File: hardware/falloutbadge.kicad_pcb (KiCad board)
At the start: 2 copper layers, 86 x 98 mm, 106 parts, among them J1 LiPo, J3 USB_C_Receptacle_USB2.0_16P, J4 E-INK, J5 Conn_01x03, Q2 Si1308EDL, Q3 AO3400A, SW1 SW_Push, SW2 SW_Push, SW3 SW_Push, SW4 SW_Push, SW5 SW_Push, T1 BALFLB-WL-09D3, U1 CH592F, U2 STM32WLE5CCUx, U3 CH9102F, U4 USBLC6-2SC6, U6 BGS12SN6, U7 AP2112K-3.3, U8 TP4056-42-ESOP8, Y1 32MHz, Y2 32MHz

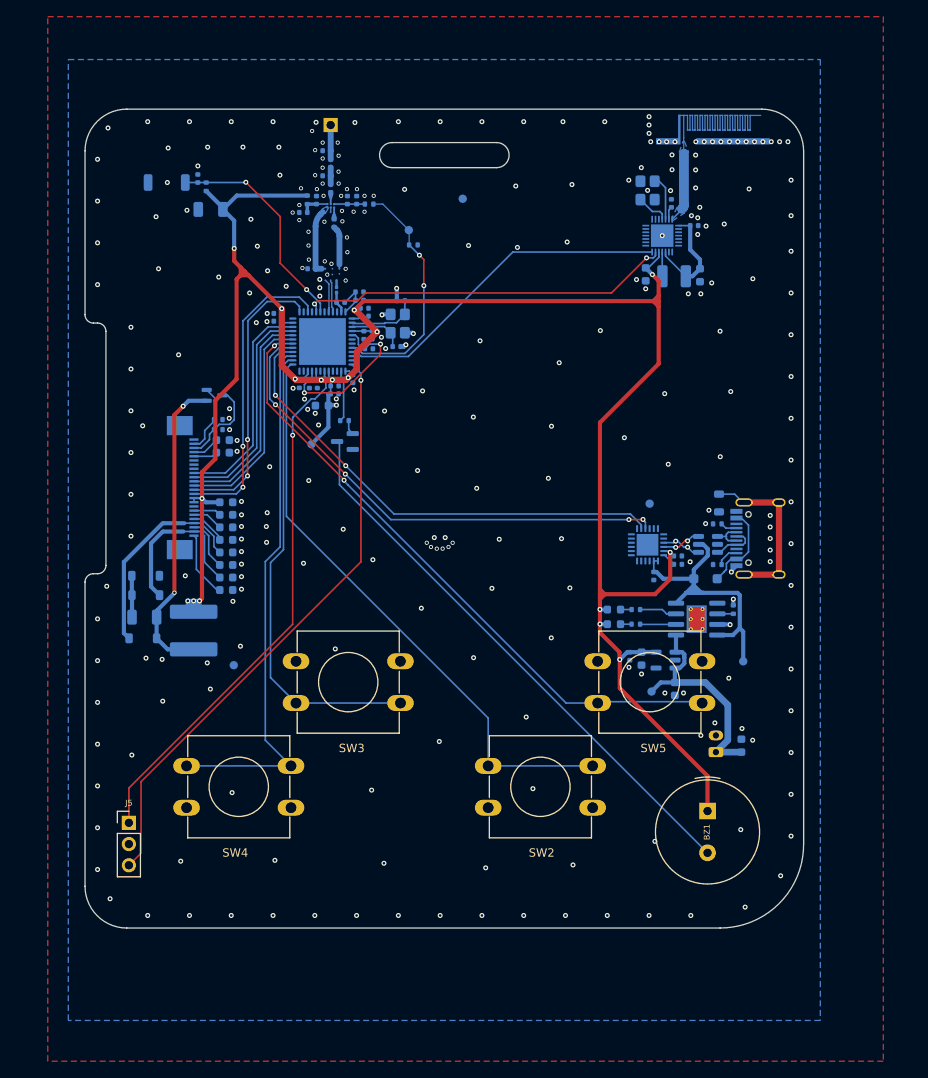
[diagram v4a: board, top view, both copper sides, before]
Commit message: add v2 w/o lora
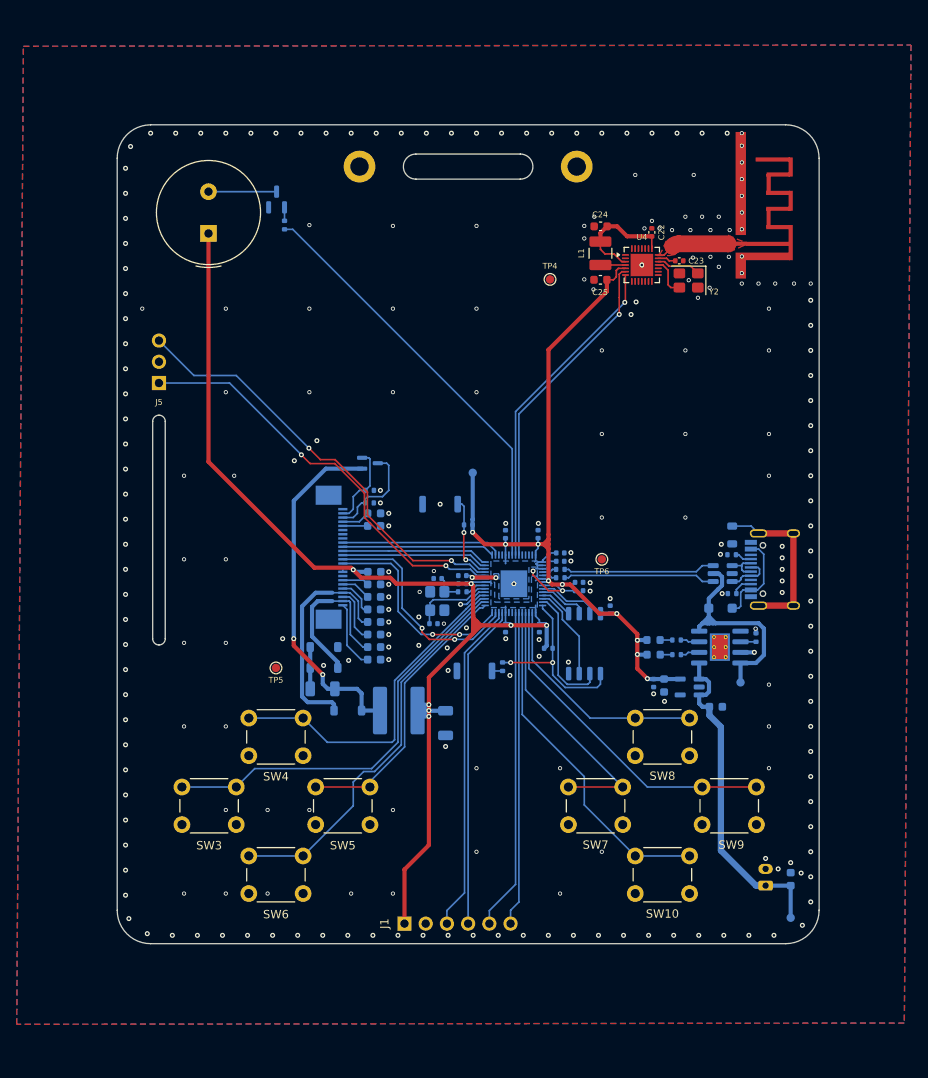
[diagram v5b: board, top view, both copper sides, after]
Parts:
- removed AE3: Antenna_Shield, antenna:ANT-F-1-2.4G-0.8mmFR4-WCH
- removed C14, C17, C18, C47, C49, C53, C54: 100nF, Capacitor_SMD:C_0402_1005Metric
- removed C19: 10uF, Capacitor_SMD:C_0603_1608Metric
- removed C20: 4.7uF, Capacitor_SMD:C_1206_3216Metric
- removed C21, C50, C52: 1uF, Capacitor_SMD:C_0402_1005Metric
- removed C42, C46, C48: 4.7uF, Capacitor_SMD:C_0603_1608Metric
- removed C43, C45: 2.2pF, Capacitor_SMD:C_0402_1005Metric
- removed C44: 1nF, Capacitor_SMD:C_0402_1005Metric
- removed C51: NC, Capacitor_SMD:C_0402_1005Metric
- removed C7: 47nF, Capacitor_SMD:C_0402_1005Metric
- removed C9: 2.2uF, Capacitor_SMD:C_0603_1608Metric
- removed D1, D2: MBR0530, Diode_SMD:D_SOD-123
- removed D4: D, Diode_SMD:D_SOD-123F
- removed D7: RED, LED_SMD:LED_0603_1608Metric
- removed L3: 68uH, Inductor_SMD:L_Changjiang_FNR6028S
- removed L4: 6.8uH, Inductor_SMD:L_0402_1005Metric
- removed L6: 10uH, Inductor_SMD:L_1210_3225Metric
- removed Q3: AO3400A, Package_TO_SOT_SMD:SOT-23
- removed R16, R17: 100R, Resistor_SMD:R_0402_1005Metric
- removed R8: 5.1k, Resistor_SMD:R_0402_1005Metric
- removed T1: BALFLB-WL-09D3, falloutbadge:CSPG-8_L2.1-W1.8_BALFHB-WL-03D3
- removed TP7: CTRL, TestPoint:TestPoint_Pad_D1.0mm
- removed U3: CH9102F, Package_DFN_QFN:QFN-24-1EP_4x4mm_P0.5mm_EP2.6x2.6mm
- removed U8: TP4056-42-ESOP8, Package_SO:SOIC-8-1EP_3.9x4.9mm_P1.27mm_EP2.41x3.3mm_ThermalVias
- added C13: 100nF, Capacitor_SMD:C_0402_1005Metric, B.Cu at (153.5, 102.0)
- added C35: 1uF, Capacitor_SMD:C_0603_1608Metric, B.Cu at (137.8, 114.0)
- added D10: MBR0530, Diode_SMD:D_SOD-123, B.Cu at (131.8, 118.0)
- added D11: MBR0530, Diode_SMD:D_SOD-123, B.Cu at (134.6, 123.1)
- added D6: RED, LED_SMD:LED_0603_1608Metric, B.Cu at (171.2, 114.7)
- added D9: MBR0530, Diode_SMD:D_SOD-123, B.Cu at (131.8, 115.5)
- added H1: MountingHole, MountingHole:MountingHole_2.2mm_M2_DIN965_Pad, F.Cu at (136.0, 58.0)
- added H2: MountingHole, MountingHole:MountingHole_2.2mm_M2_DIN965_Pad, F.Cu at (162.0, 58.0)
- added J2: USB_C_Receptacle_USB2.0_16P, Connector_USB:USB_C_Receptacle_HRO_TYPE-C-31-M-12, B.Cu at (186.9, 106.2)
- added L2: 68uH, Inductor_SMD:L_Changjiang_FNR6028S, B.Cu at (140.7, 123.1)
- added Q1: AO3400A, Package_TO_SOT_SMD:SOT-23, B.Cu at (126.1, 61.9)
- added R10: 5.1k, Resistor_SMD:R_0402_1005Metric, B.Cu at (180.6, 109.1)
- added R11: 10k, Resistor_SMD:R_0402_1005Metric, B.Cu at (137.2, 96.8)
- added R14: 330R, Resistor_SMD:R_0402_1005Metric, B.Cu at (173.9, 116.4)
- added R3: 1k, Resistor_SMD:R_0402_1005Metric, B.Cu at (148.3, 108.9)
- added R5: 27.4R, Resistor_SMD:R_0402_1005Metric, B.Cu at (160.0, 107.2)
- added SW10: SW_Push, Button_Switch_THT:SW_PUSH_6mm, F.Cu at (169.0, 140.5)
- added SW6: SW_Push, Button_Switch_THT:SW_PUSH_6mm, F.Cu at (122.8, 140.5)
- added SW7: SW_Push, Button_Switch_THT:SW_PUSH_6mm, F.Cu at (161.0, 132.2)
- added SW8: SW_Push, Button_Switch_THT:SW_PUSH_6mm, F.Cu at (169.0, 124.0)
- added SW9: SW_Push, Button_Switch_THT:SW_PUSH_6mm, F.Cu at (177.0, 132.2)
- added U5: USBLC6-2SC6, Package_TO_SOT_SMD:SOT-23-6, B.Cu at (179.5, 106.7)
- AE2: value Antenna -> Antenna_Shield; footprint Connector_PinHeader_2.54mm:PinHeader_1x01_P2.54mm_Vertical -> antenna:ANT-F-1-2.4G-1.6mmFR4-WCH; moved to F.Cu
- C1, C2: value 100nF -> 33pF
- C10: value 4.7uF -> 100nF; footprint Capacitor_SMD:C_0603_1608Metric -> Capacitor_SMD:C_0402_1005Metric
- C11: value 1uF -> 100nF
- C22: value 4.7uF -> 100nF; footprint Capacitor_SMD:C_1206_3216Metric -> Capacitor_SMD:C_0402_1005Metric; moved to F.Cu
- C23: value 100nF -> 0.47uF; moved to F.Cu
- C24: value 1uF -> 4.7uF; moved to F.Cu
- C25: value 1uF -> 2.2uF; moved to F.Cu
- C26, C27: value 1uF -> 4.7uF; footprint Capacitor_SMD:C_0603_1608Metric -> Capacitor_SMD:C_1206_3216Metric
- C3: value 0.47uF -> 100nF
- C34: value 100nF -> 1uF; footprint Capacitor_SMD:C_0402_1005Metric -> Capacitor_SMD:C_0603_1608Metric
- C36: value 100pF -> 1uF; footprint Capacitor_SMD:C_0201_0603Metric -> Capacitor_SMD:C_0603_1608Metric
- C37: value 68pF -> 1uF; footprint Capacitor_SMD:C_0402_1005Metric -> Capacitor_SMD:C_0603_1608Metric
- C38: value 10pF -> 4.7uF; footprint Capacitor_SMD:C_0402_1005Metric -> Capacitor_SMD:C_0603_1608Metric
- C39: value 10pF -> 10uF; footprint Capacitor_SMD:C_0402_1005Metric -> Capacitor_SMD:C_0603_1608Metric
- C40: value 1nF -> 4.7uF; footprint Capacitor_SMD:C_0402_1005Metric -> Capacitor_SMD:C_0603_1608Metric
- C41: value 68pF -> 100nF
- C5: value 6.8pF -> 100nF
- C6: value 6.8pF -> 1uF
- C8: value 68pF -> 1uF
- D3: value MBR0530 -> D; footprint Diode_SMD:D_SOD-123 -> Diode_SMD:D_SOD-123F
- J1: value LiPo -> Conn_02x03; footprint Connector_JST:JST_PH_S2B-PH-K_1x02_P2.00mm_Horizontal -> Connector_PinHeader_2.54mm:PinHeader_1x06_P2.54mm_Vertical; moved to F.Cu
- J3: value USB_C_Receptacle_USB2.0_16P -> E-INK; footprint Connector_USB:USB_C_Receptacle_HRO_TYPE-C-31-M-12 -> Connector_FFC-FPC:TE_2-1734839-4_1x24-1MP_P0.5mm_Horizontal
- J4: value E-INK -> LiPo; footprint Connector_FFC-FPC:TE_2-1734839-4_1x24-1MP_P0.5mm_Horizontal -> Connector_JST:JST_PH_S2B-PH-K_1x02_P2.00mm_Horizontal
- L1: value 68nH -> 10uH; footprint Inductor_SMD:L_0402_1005Metric -> Inductor_SMD:L_1210_3225Metric; moved to F.Cu
- R1: value 10k -> 330R
- R12: value 330R -> 0.47R
- R2: value 330R -> 10k
- R4: value 10k -> 27.4R
- R7: value 0.47R -> 1k
- SW1: value SW_Push -> RESET; footprint Button_Switch_SMD:SW_SPST_TS-1088-xR025 -> Button_Switch_SMD:SW_Push_SPST_NO_Alps_SKRK
- SW2: value SW_Push -> BOOTSEL; footprint Button_Switch_THT:SW_PUSH-12mm -> Button_Switch_SMD:SW_Push_SPST_NO_Alps_SKRK; moved to B.Cu
- SW3, SW4, SW5: footprint Button_Switch_THT:SW_PUSH-12mm -> Button_Switch_THT:SW_PUSH_6mm
- TP2: value GND -> VBUS
- TP3: value VBUS -> +BATT
- TP4, TP6, Y2: moved to F.Cu
- TP5: value +BATT -> GND; moved to F.Cu
- U1: value CH592F -> W25Q32JVSS; footprint Package_DFN_QFN:WQFN-28-1EP_4x4mm_P0.4mm_EP2.7x2.7mm -> Package_SO:SOIC-8_5.3x5.3mm_P1.27mm
- U2: value STM32WLE5CCUx -> RP2040; footprint footprints:UFQFPN-48_L7.0-W7.0-P0.50-BL-EP5.6 -> Package_DFN_QFN:QFN-56-1EP_7x7mm_P0.4mm_EP3.2x3.2mm
- U4: value USBLC6-2SC6 -> CH592F; footprint Package_TO_SOT_SMD:SOT-23-6 -> Package_DFN_QFN:WQFN-28-1EP_4x4mm_P0.4mm_EP2.7x2.7mm; moved to F.Cu
- U6: value BGS12SN6 -> TP4056-42-ESOP8; footprint Package_LGA:Infineon_PG-TSNP-6-10_0.7x1.1mm_0.7x1.1mm_P0.4mm -> Package_SO:SOIC-8-1EP_3.9x4.9mm_P1.27mm_EP2.41x3.3mm_ThermalVias
- Y1: value 32MHz -> 12MHz
- moved C39 97.0 mm to (187.6, 143.3)
- moved BZ1 91.4 mm to (117.9, 66.0), turned to 90 degrees
- moved J4 84.5 mm to (184.6, 144.1)
- moved C38 77.2 mm to (178.7, 122.7), turned to 180 degrees
- moved C22 76.2 mm to (171.0, 65.9), turned to -90 degrees
- moved C4 71.4 mm to (166.0, 111.0), turned to 90 degrees
- moved C40 71.2 mm to (172.4, 120.1), turned to 90 degrees
- moved C41 70.7 mm to (171.2, 119.8)
- moved U6 70.4 mm to (179.1, 115.5), turned to 180 degrees
- moved D3 69.2 mm to (179.2, 110.8)
- moved C24 55.7 mm to (164.9, 65.2)
- moved J5 52.8 mm to (112.0, 83.9), turned to 180 degrees
- moved J3 52.5 mm to (132.7, 104.8), turned to 90 degrees
- moved C37 52.4 mm to (137.8, 117.0), turned to 180 degrees
- moved C2 52.2 mm to (145.4, 107.3), turned to 0 degrees
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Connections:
- C1 pad 1: +3V3 -> GND
- C1 pad 2: GND -> Net-(U2-XIN)
- C10 pad 1: /VDCIA -> +3V3
- C12 pad 1: GND -> +3V3
- C12 pad 2: /VFBSMPS -> GND
- C16 pad 1: /VFBSMPS -> +3V3
- C2 pad 2: /VDCIA -> Net-(C2-Pad2)
- C22 pad 1: Net-(D1-A) -> GND
- C22 pad 2: Net-(D3-A) -> /VDCIA
- C23 pad 1: Net-(U3-V3) -> GND
- C23 pad 2: GND -> Net-(U4-VINTA)
- C24 pad 1: GND -> /VDCIA
- C24 pad 2: +3V3 -> GND
- C25 pad 2: Net-(J4-Pin_21) -> +3V3
- C26 pad 1: GND -> +3V3
- C26 pad 2: Net-(J4-Pin_20) -> GND
- C27 pad 1: GND -> Net-(D10-K)
- C27 pad 2: Net-(J4-Pin_7) -> Net-(D11-A)
- C28 pad 2: Net-(J4-Pin_6) -> +3V3
- C29 pad 2: Net-(J4-Pin_5) -> Net-(J3-Pin_21)
- C3 pad 1: GND -> +1V1
- C3 pad 2: Net-(U1-VINTA) -> GND
- C30 pad 2: /PREVGH -> Net-(J3-Pin_20)
- C31 pad 2: Net-(J4-Pin_3) -> Net-(J3-Pin_7)
- C32 pad 2: /PREVGL -> Net-(J3-Pin_6)
- C33 pad 2: Net-(J4-Pin_1) -> Net-(J3-Pin_5)
- C34 pad 1: +3V3 -> GND
- C34 pad 2: GND -> /PREVGH
- C36 pad 1: /RFO_HP -> GND
- C36 pad 2: Net-(T1-RFO_in) -> /PREVGL
- C37 pad 1: Net-(U6-RF2) -> GND
- C37 pad 2: /C1 -> Net-(J3-Pin_1)
- C38 pad 1: Net-(U6-VDD) -> GND
- C38 pad 2: GND -> +BATT
- C39 pad 1: Net-(U6-CTRL) -> +BATT
- C4 pad 1: GND -> +3V3
- C4 pad 2: Net-(U2-NRST) -> GND
- C40 pad 1: Net-(U6-VDD) -> GND
- C40 pad 2: GND -> +3V3
- C41 pad 1: Net-(C41-Pad1) -> +3V3
- C41 pad 2: Net-(U6-RFIN) -> GND
- C5 pad 1: GND -> +1V1
- C5 pad 2: Net-(U2-OSC_IN) -> GND
- C6 pad 1: GND -> +1V1
- C6 pad 2: Net-(U2-OSC_OUT) -> GND
- C8 pad 1: GND -> +3V3
- C8 pad 2: /VR_PA -> GND
- D3 pad 1: /PREVGH -> VBUS
- FB1 pad 1: Net-(J3-SHIELD) -> Net-(J2-SHIELD)
- J1 pad 1: +BATT -> +3V3
- J4 pad 1: Net-(J4-Pin_1) -> +BATT
- J4 pad 2: /PREVGL -> GND
- L1 pad 1: /VR_PA -> /VSW
- L1 pad 2: /RFO_HP -> /VDCIA
- Q2 pad 1: Net-(D3-A) -> Net-(D11-A)
- R1 pad 1: +3V3 -> /BUZ
- R1 pad 2: Net-(U2-NRST) -> Net-(Q1-G)
- R12 pad 1: Net-(D7-K) -> /RESE
- R12 pad 2: Net-(U8-~{CHRG}) -> GND
- R13 pad 1: Net-(D8-K) -> Net-(D6-K)
- R13 pad 2: Net-(U8-~{STDBY}) -> Net-(U6-~{CHRG})
- R15 pad 1: Net-(U8-PROG) -> Net-(U6-PROG)
- R2 pad 1: /PC13 -> +3V3
- R2 pad 2: Net-(Q3-G) -> Net-(U2-RUN)
- R4 pad 1: /CTRL -> /D-
- R4 pad 2: GND -> Net-(U2-USB_DM)
- R6 pad 1: /GDR -> +3V3
- R6 pad 2: GND -> /QSPI_SS
- R7 pad 1: /RESE -> Net-(R7-Pad1)
- R7 pad 2: GND -> /QSPI_SS
- R9 pad 1: Net-(J3-CC2) -> Net-(J2-CC1)
- SW1 pad 2: Net-(U2-NRST) -> Net-(U2-RUN)
- SW2 pad 1: /PB3 -> GND
- SW2 pad 2: GND -> Net-(R7-Pad1)
- SW3 pad 1: /PB4 -> /BTN1
- SW4 pad 1: /PB5 -> /BTN2
- SW5 pad 1: /PB8 -> /BTN3
- TP2 pad 1: GND -> VBUS
- TP3 pad 1: VBUS -> +BATT
- TP5 pad 1: +BATT -> GND
- U1 pad 1: unconnected-(U1-PA11-Pad1) -> /QSPI_SS
- U1 pad 2: unconnected-(U1-PA10-Pad2) -> /QSPI_SD1
- U1 pad 3: /VDCIA -> /QSPI_SD2
- U1 pad 4: /VSW -> GND
- U1 pad 5: +3V3 -> /QSPI_SD0
- U1 pad 6: /UART1_RX -> /QSPI_SCK
- U1 pad 7: /UART1_TX -> /QSPI_SD3
- U1 pad 8: unconnected-(U1-PB15-Pad8) -> +3V3
- U2 pad 1: /PB3 -> +3V3
- U2 pad 10: /BUSY -> +3V3
- U2 pad 11: +3V3 -> /SDA
- U2 pad 12: unconnected-(U2-PA4-Pad12) -> /SCL
- U2 pad 14: unconnected-(U2-PA6-Pad14) -> /SPI_MOSI
- U2 pad 15: /SPI_MOSI -> /BTN3
- U2 pad 16: unconnected-(U2-PA8-Pad16) -> /BTN4
- U2 pad 17: /UART1_RX -> /BTN1
- U2 pad 18: Net-(U2-NRST) -> /BTN2
- U2 pad 19: unconnected-(U2-PH3-Pad19) -> GND
- U2 pad 2: /PB4 -> /BTN6
- U2 pad 20: /RFI_P -> Net-(U2-XIN)
- U2 pad 21: /RFI_N -> Net-(U2-XOUT)
- U2 pad 22: unconnected-(U2-RFO_LP-Pad22) -> +3V3
- U2 pad 23: /RFO_HP -> +1V1
- U2 pad 24: /VR_PA -> /SWCLK
- U2 pad 25: +3V3 -> /SWDIO
- U2 pad 26: Net-(U2-OSC_IN) -> Net-(U2-RUN)
- U2 pad 27: Net-(U2-OSC_OUT) -> /CS
- U2 pad 28: +3V3 -> /DC
- U2 pad 29: /VFBSMPS -> /RST
- U2 pad 3: /PB5 -> /BTN7
- U2 pad 30: unconnected-(U2-PB0-Pad30) -> /BUSY
- U2 pad 31: unconnected-(U2-PB2-Pad31) -> GND
- U2 pad 32: /CTRL -> unconnected-(U2-GPIO21-Pad32)
- U2 pad 33: /UART1_TX -> +3V3
- U2 pad 35: unconnected-(U2-PA12-Pad35) -> /BUZ
- U2 pad 36: /SWDIO -> /UART1_TX
- U2 pad 37: +3V3 -> /UART1_RX
- U2 pad 38: /PC13 -> unconnected-(U2-GPIO26/ADC0-Pad38)
- U2 pad 4: /RXD -> /BTN5
- U2 pad 41: +3V3 -> unconnected-(U2-GPIO29/ADC3-Pad41)
- U2 pad 42: /SWCLK -> +3V3
- U2 pad 43: unconnected-(U2-PA15-Pad43) -> +3V3
- U2 pad 45: /VFBSMPS -> +1V1
- U2 pad 46: +3V3 -> Net-(U2-USB_DM)
- U2 pad 47: unconnected-(U2-VLXSMPS-Pad47) -> Net-(U2-USB_DP)
- U2 pad 48: GND -> +3V3
- U2 pad 49: GND -> +3V3
- U2 pad 5: /TXD -> /BTN8
- U2 pad 6: /PB8 -> /GPIO4
- U2 pad 7: /CS -> /GPIO5
- U2 pad 8: /DC -> unconnected-(U2-GPIO6-Pad8)
- U2 pad 9: /RST -> unconnected-(U2-GPIO7-Pad9)
- U4 pad 1: Net-(J3-D--PadA7) -> unconnected-(U4-PA11-Pad1)
- U4 pad 2: GND -> unconnected-(U4-PA10-Pad2)
- U4 pad 3: Net-(J3-D+-PadA6) -> /VDCIA
- U4 pad 4: /D+ -> /VSW
- U4 pad 5: VBUS -> +3V3
- U4 pad 6: /D- -> /UART1_RX
- U6 pad 1: Net-(U6-RF2) -> GND
- U6 pad 2: GND -> Net-(U6-PROG)
- U6 pad 3: Net-(T1-RFI_in) -> GND
- U6 pad 4: Net-(U6-VDD) -> VBUS
- U6 pad 5: Net-(U6-RFIN) -> +BATT
- U6 pad 6: Net-(U6-CTRL) -> Net-(U6-~{STDBY})
- Y1 pad 1: Net-(U2-OSC_IN) -> Net-(U2-XIN)
- Y1 pad 3: Net-(U2-OSC_OUT) -> Net-(C2-Pad2)
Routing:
- net /PB8: track 76.6 -> 0.00 mm, vias 2 -> 0
- net /PB3: track 71.0 -> 0.00 mm
- net /PB5: track 64.6 -> 0.00 mm
- net /TXD: track 60.1 -> 0.00 mm, vias 4 -> 0
- net Net-(BZ1--): track 67.6 -> 8.15 mm
- net /RXD: track 57.7 -> 0.00 mm, vias 2 -> 0
- net /PB4: track 56.2 -> 0.00 mm
- net /BUZ: track 0.00 -> 50.8 mm
- net /BTN1: track 0.00 -> 49.9 mm
- net /BTN4: track 0.00 -> 46.9 mm
- net Net-(D11-A): track 0.00 -> 42.5 mm, vias 0 -> 2
- net /BTN8: track 0.00 -> 41.2 mm
- net /BTN2: track 0.00 -> 40.9 mm
- net /SCL: track 0.00 -> 39.8 mm
- net /BTN7: track 0.00 -> 39.8 mm
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- added copper zone on B.Cu, net +1V1
- added copper zone on B.Cu, net +3V3
- added copper zone on F.Cu, net Net-(AE2-A)
- removed copper zone on B.Cu, net Net-(AE3-A)
- removed copper zone on B.Cu, net Net-(T1-RFI_in)
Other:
- board size 86 x 98 mm -> 84 x 98 mm
- board text removed: "FALLOUT"
- board text removed: "July 1 - 7, 2026"

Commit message: final board for prod
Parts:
- added R16: 4k7, Resistor_SMD:R_0402_1005Metric, B.Cu at (148.8, 143.5)
- added R17: 4k7, Resistor_SMD:R_0402_1005Metric, B.Cu at (146.8, 141.5)
- BOOTSEL: renamed from SW2; footprint Button_Switch_SMD:SW_Push_SPST_NO_Alps_SKRK -> footprints:KEY-SMD_K2-1177SW-A4DW-06
- GND: renamed from TP6; moved to B.Cu
- GND: renamed from TP5; moved to B.Cu
- GND: renamed from TP4; moved to B.Cu
- R15: value 3.3k -> 2.2k
- RESET: renamed from SW1; footprint Button_Switch_SMD:SW_Push_SPST_NO_Alps_SKRK -> footprints:KEY-SMD_K2-1177SW-A4DW-06
- moved C26 6.56 mm to (141.1, 128.6), turned to 180 degrees
- moved BOOTSEL 4.02 mm to (152.0, 121.7), turned to 90 degrees
- moved J5 3.47 mm to (112.2, 80.4)
- moved C27 3.42 mm to (134.6, 122.0)
- moved +BATT 1.88 mm to (187.6, 146.0)
- moved C28 1.85 mm to (137.8, 108.3)
- moved C29 1.85 mm to (137.8, 101.3)
- moved C30 1.85 mm to (137.8, 102.8)
- moved C31 1.85 mm to (137.8, 109.8)
- moved C32 1.85 mm to (137.8, 111.3)
- moved C33 1.85 mm to (137.8, 112.8)
- moved C34 1.85 mm to (137.8, 114.3)
- moved C35 1.85 mm to (137.8, 115.8)
- moved C36 1.85 mm to (137.8, 117.3)
- moved C37 1.85 mm to (137.8, 118.8)
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- renumbered TP1 to +3V3, TP2 to +5V, TP3 to +BATT
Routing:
- net +3V3: track 249.6 -> 261.4 mm, vias 16 -> 19
- net /BTN2: track 40.9 -> 47.7 mm
- net /BTN3: track 34.1 -> 38.6 mm
- net /BTN4: track 46.9 -> 51.0 mm
- net /BTN1: track 49.9 -> 53.8 mm
- net /PREVGH: track 26.9 -> 24.7 mm
- net +BATT: track 39.9 -> 38.0 mm
- net /SPI_SCK: track 26.9 -> 25.1 mm
- net /SPI_MOSI: track 25.5 -> 23.6 mm
- net Net-(D10-K): track 5.00 -> 6.59 mm
- net Net-(D11-A): track 42.5 -> 41.0 mm
- net /DC: track 17.6 -> 18.7 mm
- net +1V1: track 17.2 -> 18.1 mm, vias 4 -> 6
- net /CS: track 17.5 -> 18.3 mm
- net /RST: track 18.3 -> 19.0 mm
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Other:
- outline, holes or cut-outs redrawn
